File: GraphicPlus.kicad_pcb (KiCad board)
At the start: 2 copper layers, 100 x 77.5 mm, 23 parts, among them J1 Apple II Expansion Bus, J2 Printer Connector, Q1 Q_NPN_EBC, SW1 SW_DIP_x04, U1 74LS00, U10 74LS373, U11 74LS373, U2 74LS279, U3 74LS02, U4 74LS00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

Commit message: native 374 version
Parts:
- removed Q1: Q_NPN_EBC, Package_TO_SOT_THT:TO-92
- removed R2: 4.7K, Resistor_THT:R_Axial_DIN0207_L6.3mm_D2.5mm_P10.16mm_Horizontal
- removed U4: 74LS00, Package_DIP:DIP-14_W7.62mm
- added C7: C, Capacitor_THT:C_Rect_L7.0mm_W2.0mm_P5.00mm, F.Cu at (122.5, 73.7)
- added C8: C, Capacitor_THT:C_Rect_L7.0mm_W2.0mm_P5.00mm, F.Cu at (178.4, 102.9)
- C1: value C -> 100p
- C3: value C -> 470p
- D1: footprint Diode_THT:D_A-405_P10.16mm_Horizontal -> Diode_THT:D_A-405_P7.62mm_Horizontal
- U9: value 2732 -> 2764; footprint Package_DIP:DIP-24_W15.24mm -> Package_DIP:DIP-28_W15.24mm
- moved C2 57.0 mm to (133.9, 71.1), turned to 180 degrees
- moved C4 7.41 mm to (141.6, 123.2)
- moved C3 5.16 mm to (133.9, 99.1), turned to 180 degrees
- moved C6 1.31 mm to (186.1, 102.9), turned to -90 degrees
- moved U1 1.27 mm to (114.9, 80.0)
- moved C1 1.27 mm to (121.2, 100.3)
- moved U2 1.27 mm to (127.6, 76.2)
- moved U6 1.27 mm to (114.9, 105.4)
- moved U7 1.27 mm to (127.6, 104.1)
- moved U9 1.27 mm to (158.1, 95.2)
- moved SW1 1.26 mm to (203.8, 111.8)
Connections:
- net Net-(U2D-~{S1}) renamed /~{BANK2}
- U1 pad 1: /A2 -> Net-(C1-Pad1)
- U1 pad 2: Net-(C1-Pad1) -> Net-(U1-Pad2)
- U1 pad 3: Net-(U2A-~{R}) -> /~{OUTPUT}
- U1 pad 4: Net-(C1-Pad1) -> /~{DEV}
- U1 pad 5: /A1 -> /~{DEV}
- U1 pad 6: Net-(U2A-~{S1}) -> Net-(U1-Pad6)
- U10 pad 11: Net-(U10-LE) -> /G_OUTPUT
- U11 pad 18: /IRQ -> +5V
- U2 pad 1: Net-(U2A-~{R}) -> +5V
- U2 pad 10: Net-(U2C-~{R}) -> /~{OUTPUT}
- U2 pad 2: Net-(U2A-~{S1}) -> +5V
- U2 pad 3: /~{RST} -> +5V
- U2 pad 4: Net-(U2A-Q) -> unconnected-(U2A-Q-Pad4)
- U3 pad 10: Net-(U3-Pad10) -> Net-(U1-Pad2)
- U3 pad 11: Net-(U3-Pad11) -> /Q3
- U3 pad 12: Net-(U2A-Q) -> /~{OUTPUT}
- U3 pad 13: /IRQ -> /G_OUTPUT
- U5 pad 2: Net-(U2C-~{R}) -> /~{OUTPUT}
- U6 pad 1: /ACK -> /R/~{W}
- U6 pad 2: /ACK -> Net-(U1-Pad6)
- U6 pad 3: Net-(U3-Pad11) -> Net-(U11-OE)
- U9 pad 1: /A7 -> +5V
- U9 pad 10: /D1 -> /A0
- U9 pad 11: /D2 -> /D0
- U9 pad 12: GND -> /D1
- U9 pad 13: /D3 -> /D2
- U9 pad 14: /D4 -> GND
- U9 pad 15: /D5 -> /D3
- U9 pad 16: /D6 -> /D4
- U9 pad 17: /D7 -> /D5
- U9 pad 18: /~{ROMEN} -> /D6
- U9 pad 19: /ROMA10 -> /D7
- U9 pad 2: /ROMA6 -> GND
- U9 pad 21: /ROMA11 -> /ROMA10
- U9 pad 22: /ROMA9 -> GND
- U9 pad 23: /ROMA8 -> /ROMA11
- U9 pad 24: +5V -> /ROMA9
- U9 pad 3: /A5 -> /A7
- U9 pad 4: /A4 -> /ROMA6
- U9 pad 5: /A3 -> /A5
- U9 pad 6: /A2 -> /A4
- U9 pad 7: /A1 -> /A3
- U9 pad 8: /A0 -> /A2
- U9 pad 9: /D0 -> /A1
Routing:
- net /A2: track 119.8 -> 34.0 mm, vias 1 -> 0
- net /Q3: track 0.00 -> 80.4 mm, vias 0 -> 2
- net /IRQ: track 70.1 -> 0.00 mm
- net /~{OUTPUT}: track 0.00 -> 61.2 mm, vias 0 -> 1
- net Net-(U11-OE): track 45.3 -> 104.6 mm, vias 0 -> 2
- net Net-(U3-Pad11): track 56.4 -> 0.00 mm, vias 1 -> 0
- net /G_OUTPUT: track 0.00 -> 49.8 mm, vias 0 -> 1
- net Net-(U2C-~{R}): track 45.3 -> 0.00 mm
- net /R/~{W}: track 116.5 -> 160.9 mm, vias 1 -> 2
- net /~{DEV}: track 85.8 -> 123.6 mm, vias 2 -> 3
- net Net-(U1-Pad2): track 0.00 -> 37.1 mm
- net /A1: track 98.5 -> 62.1 mm
- net Net-(U10-LE): track 32.8 -> 0.00 mm
- net /ACK: track 102.6 -> 69.8 mm
- net Net-(Q1-B): track 30.6 -> 0.00 mm
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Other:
- board text added: "Graphic+"
- board text added: "Printer Interface"
- board text added: "github.com/btb/GraphicPlus"
- board text added: "rev ${REVISION}"
- board text removed: "Graphic +"

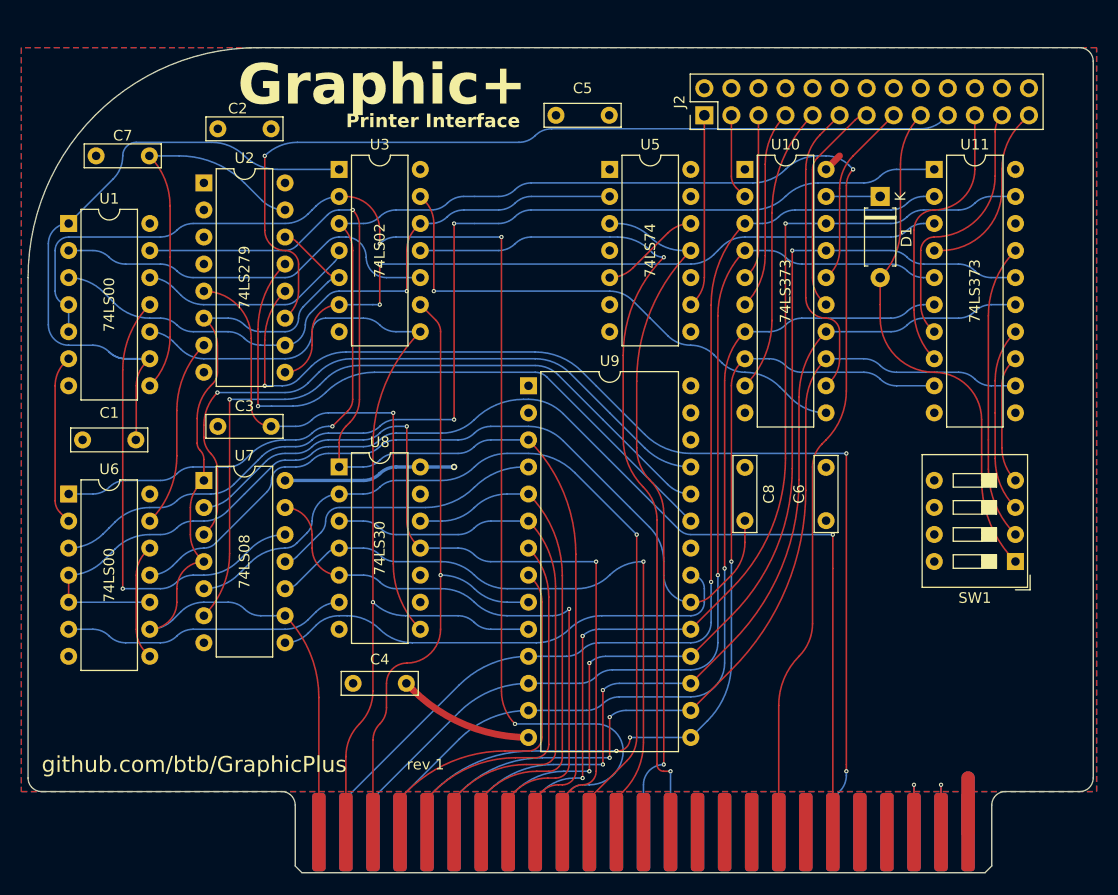
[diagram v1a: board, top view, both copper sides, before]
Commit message: consolidate 74ls00 chips, better spacing
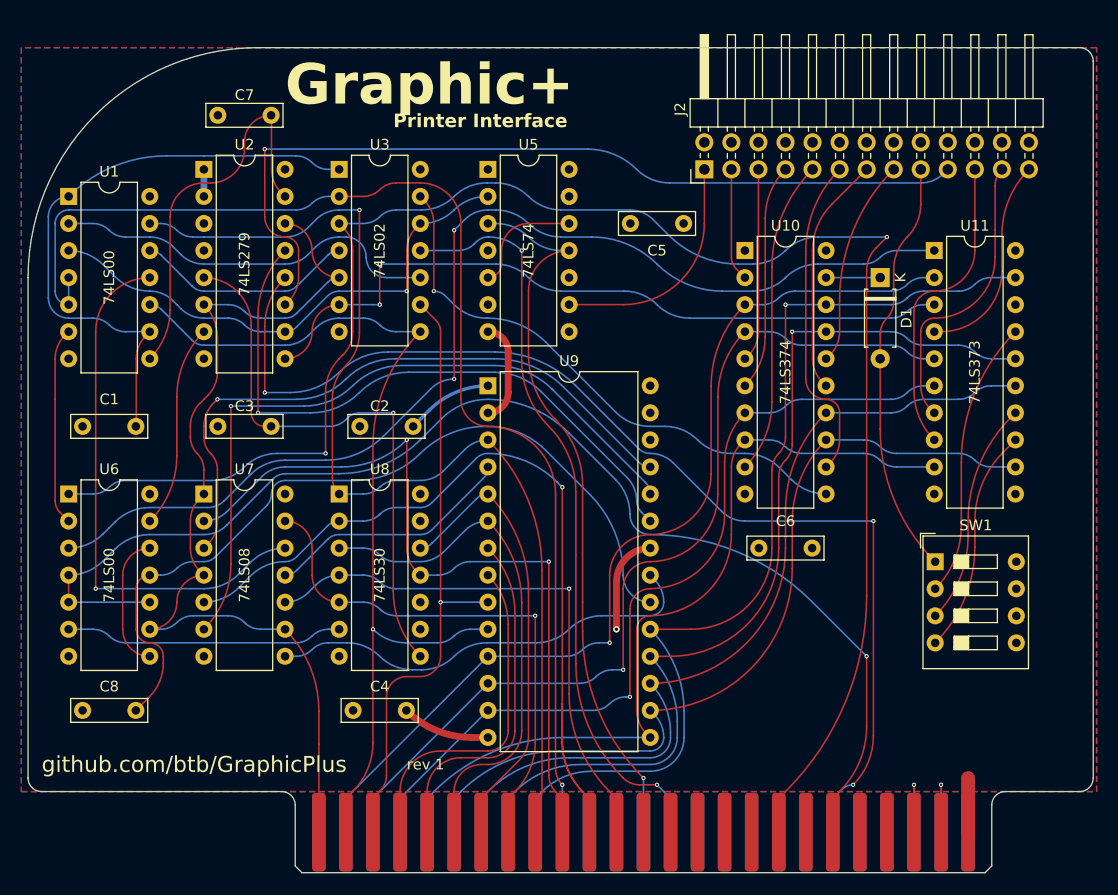
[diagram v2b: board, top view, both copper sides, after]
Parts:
- J2: footprint Connector_PinHeader_2.54mm:PinHeader_2x13_P2.54mm_Vertical -> Connector_PinHeader_2.54mm:PinHeader_2x13_P2.54mm_Horizontal
- U10: value 74LS373 -> 74LS374
- moved C8 66.2 mm to (116.2, 125.7), turned to 0 degrees
- moved C2 31.0 mm to (147.3, 99.1)
- moved C7 12.0 mm to (133.9, 69.8)
- moved U5 11.4 mm to (154.3, 74.9)
- moved C5 10.4 mm to (167.7, 80.0), turned to 0 degrees
- moved C6 7.69 mm to (184.7, 110.5), turned to 180 degrees
- moved D1 7.62 mm to (191.1, 85.1)
- moved U10 7.62 mm to (178.4, 82.5)
- moved U11 7.62 mm to (196.2, 82.5)
- moved SW1 7.54 mm to (196.3, 111.8), turned to 0 degrees
- moved J2 5.08 mm to (174.6, 74.9)
- moved U9 3.81 mm to (154.3, 95.2)
- moved C4 2.54 mm to (141.6, 125.7)
- moved U1 2.54 mm to (114.9, 77.5)
- moved U8 2.54 mm to (140.3, 105.4)
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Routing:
- net GND: track 17.9 -> 32.3 mm, vias 0 -> 1
- net /~{OUTPUT}: track 61.2 -> 49.1 mm
- net /A10: track 62.8 -> 51.7 mm
- net /D0: track 100.5 -> 89.8 mm
- net /D1: track 97.1 -> 87.0 mm
- net /Q3: track 80.4 -> 70.3 mm
- net /D2: track 88.6 -> 78.8 mm
- net /PD7: track 48.7 -> 39.1 mm
- net /~{DEV}: track 123.6 -> 114.3 mm, vias 3 -> 1
- net Net-(U11-D4): track 12.1 -> 21.1 mm
- net /D3: track 85.5 -> 77.4 mm, vias 3 -> 0
- net +5V: track 23.1 -> 15.9 mm, vias 1 -> 0
- net Net-(U1-Pad11): track 44.0 -> 50.8 mm
- net /D4: track 85.7 -> 79.3 mm, vias 2 -> 0
- net /A6: track 56.5 -> 50.1 mm
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
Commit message: finish up rev 1
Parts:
- added U9Alt1: 2732, Package_DIP:DIP-24_W15.24mm, F.Cu at (156.8, 100.3)
- C2, C4, C5, C6: value C -> 100n
- C7: value C -> 100p
- moved C8 66.1 mm to (170.2, 87.6)
- moved U5 3.59 mm to (156.8, 72.4)
- moved C5 3.59 mm to (170.2, 82.5)
- moved C3 2.54 mm to (136.5, 99.1)
- moved C7 2.54 mm to (136.5, 69.8)
- moved D1 2.54 mm to (193.7, 85.1)
- moved U2 2.54 mm to (130.2, 74.9)
- moved U7 2.54 mm to (130.2, 105.4)
- moved C1 2.54 mm to (123.8, 99.1)
- moved C2 2.54 mm to (149.8, 99.1)
- moved C4 2.54 mm to (144.2, 125.7)
- moved C6 2.54 mm to (187.3, 110.5)
- moved S1 2.54 mm to (198.8, 111.8)
- moved U1 2.54 mm to (117.5, 77.5)
- moved U10 2.54 mm to (181.0, 82.5)
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- renumbered SW1 to S1
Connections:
- U1 pad 10: /A0 -> Net-(U2B-Q)
- U1 pad 2: Net-(U1-Pad2) -> /A0
- U1 pad 3: /~{OUTPUT} -> /~{BANK2}
- U1 pad 4: /~{DEV} -> /~{IOSEL}
- U1 pad 5: /~{DEV} -> /~{IOSTB}
- U1 pad 8: /~{BANK2} -> /~{ROMEN}
- U1 pad 9: Net-(C1-Pad1) -> Net-(U1-Pad6)
- U2 pad 2: +5V -> /~{IOSTB}
- U2 pad 3: +5V -> /~{IOSTB}
- U2 pad 4: unconnected-(U2A-Q-Pad4) -> Net-(U2A-Q)
- U3 pad 10: Net-(U1-Pad2) -> Net-(U3-Pad10)
- U6 pad 1: /R/~{W} -> Net-(U6-Pad1)
- U6 pad 10: /~{IOSTB} -> +5V
- U6 pad 11: /~{ROMEN} -> /~{OUTPUT}
- U6 pad 12: Net-(U6-Pad12) -> Net-(C1-Pad1)
- U6 pad 13: Net-(U2B-Q) -> Net-(U3-Pad10)
- U6 pad 2: Net-(U1-Pad6) -> /R/~{W}
- U6 pad 4: /~{IOSTB} -> /~{DEV}
- U6 pad 5: /~{IOSTB} -> /~{DEV}
- U6 pad 6: Net-(U6-Pad6) -> Net-(U6-Pad1)
- U6 pad 8: Net-(U6-Pad12) -> unconnected-(U6-Pad8)
- U6 pad 9: /~{IOSEL} -> +5V
- U8 pad 6: Net-(U6-Pad6) -> Net-(U2A-Q)
- U9 pad 20: /~{ROMEN} -> GND
- U9 pad 22: GND -> /~{ROMEN}
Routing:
- net Net-(U3-Pad10): track 0.00 -> 59.6 mm, vias 0 -> 1
- net Net-(U2A-Q): track 0.00 -> 49.7 mm, vias 0 -> 1
- net Net-(U1-Pad2): track 36.9 -> 0.00 mm
- net /~{IOSTB}: track 117.3 -> 148.3 mm
- net Net-(U6-Pad6): track 26.0 -> 0.00 mm
- net /~{OUTPUT}: track 49.1 -> 71.7 mm, vias 1 -> 2
- net /~{ROMEN}: track 76.5 -> 97.8 mm, vias 0 -> 1
- net GND: track 32.3 -> 13.4 mm, vias 1 -> 0
- net /A0: track 88.1 -> 104.3 mm, vias 1 -> 2
- net Net-(U6-Pad1): track 0.00 -> 14.0 mm
- net Net-(U2B-Q): track 19.1 -> 5.84 mm
- net Net-(U6-Pad12): track 12.9 -> 0.00 mm
- net Net-(U1-Pad6): track 18.6 -> 7.62 mm
- net +5V: track 15.9 -> 5.08 mm
- net /A9: track 81.1 -> 71.2 mm
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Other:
- board text added: "JLCJLCJLCJLC"
- board text added: "locked"
- board text removed: "github.com/btb/GraphicPlus"
